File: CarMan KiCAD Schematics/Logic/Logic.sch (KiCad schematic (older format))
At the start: 50 parts, among them J1 Motor Controller Can Line, J2 NON-ISO I2C Testing Header, J3 Logic-TSI Connector, J4 GLV BOB, J5 PIC program, J6 NON-ISO CAN Testing, J7 You're Welcome -Ethan, U1 MCP9700AT-HTT-Sensor_Temperat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, U10 BNO_055, U11 Raspberry_Pi_RTC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

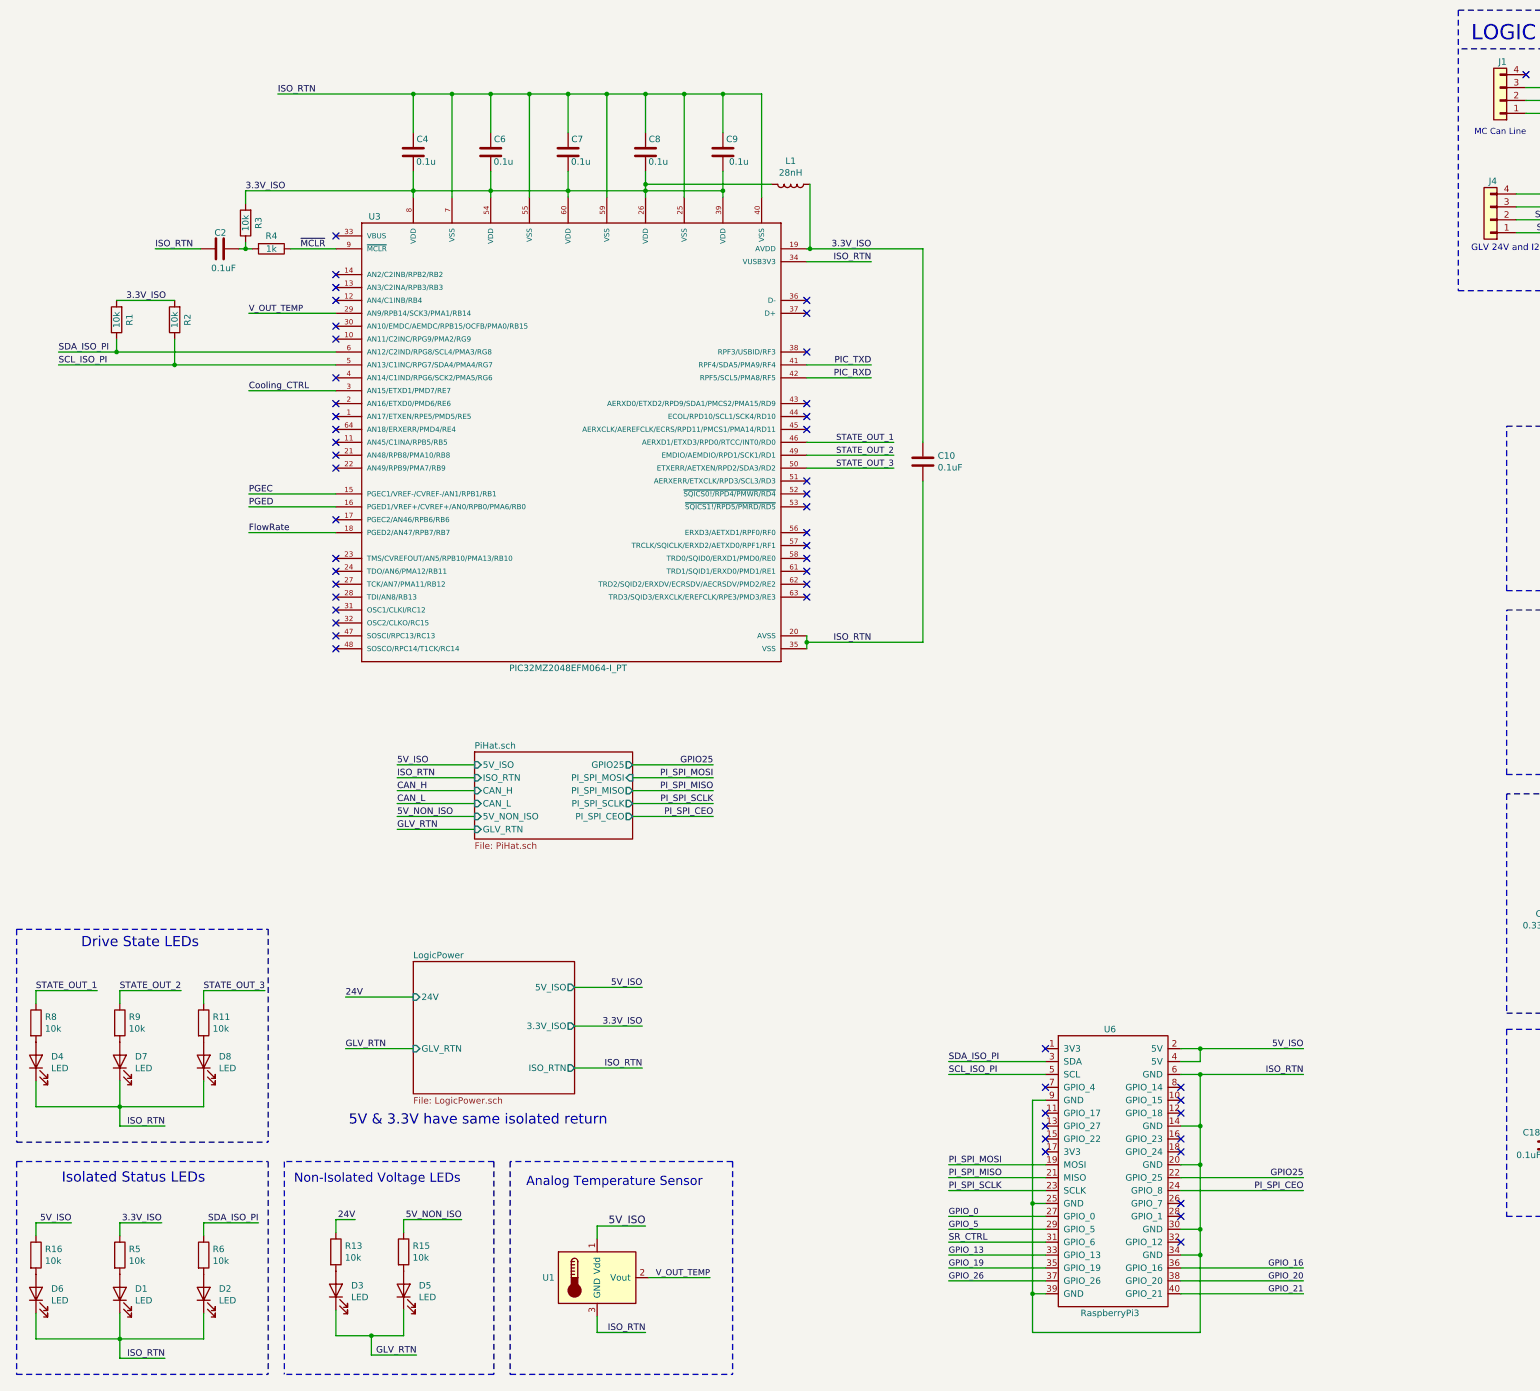
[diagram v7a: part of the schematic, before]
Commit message: -Added buttons across coils (instead of jumpers) for the AMS & IMD relays - Added push button for RTDS testing - Added a header (Currently J22) such that we can hook up a SPDT switch and change direction car is driving
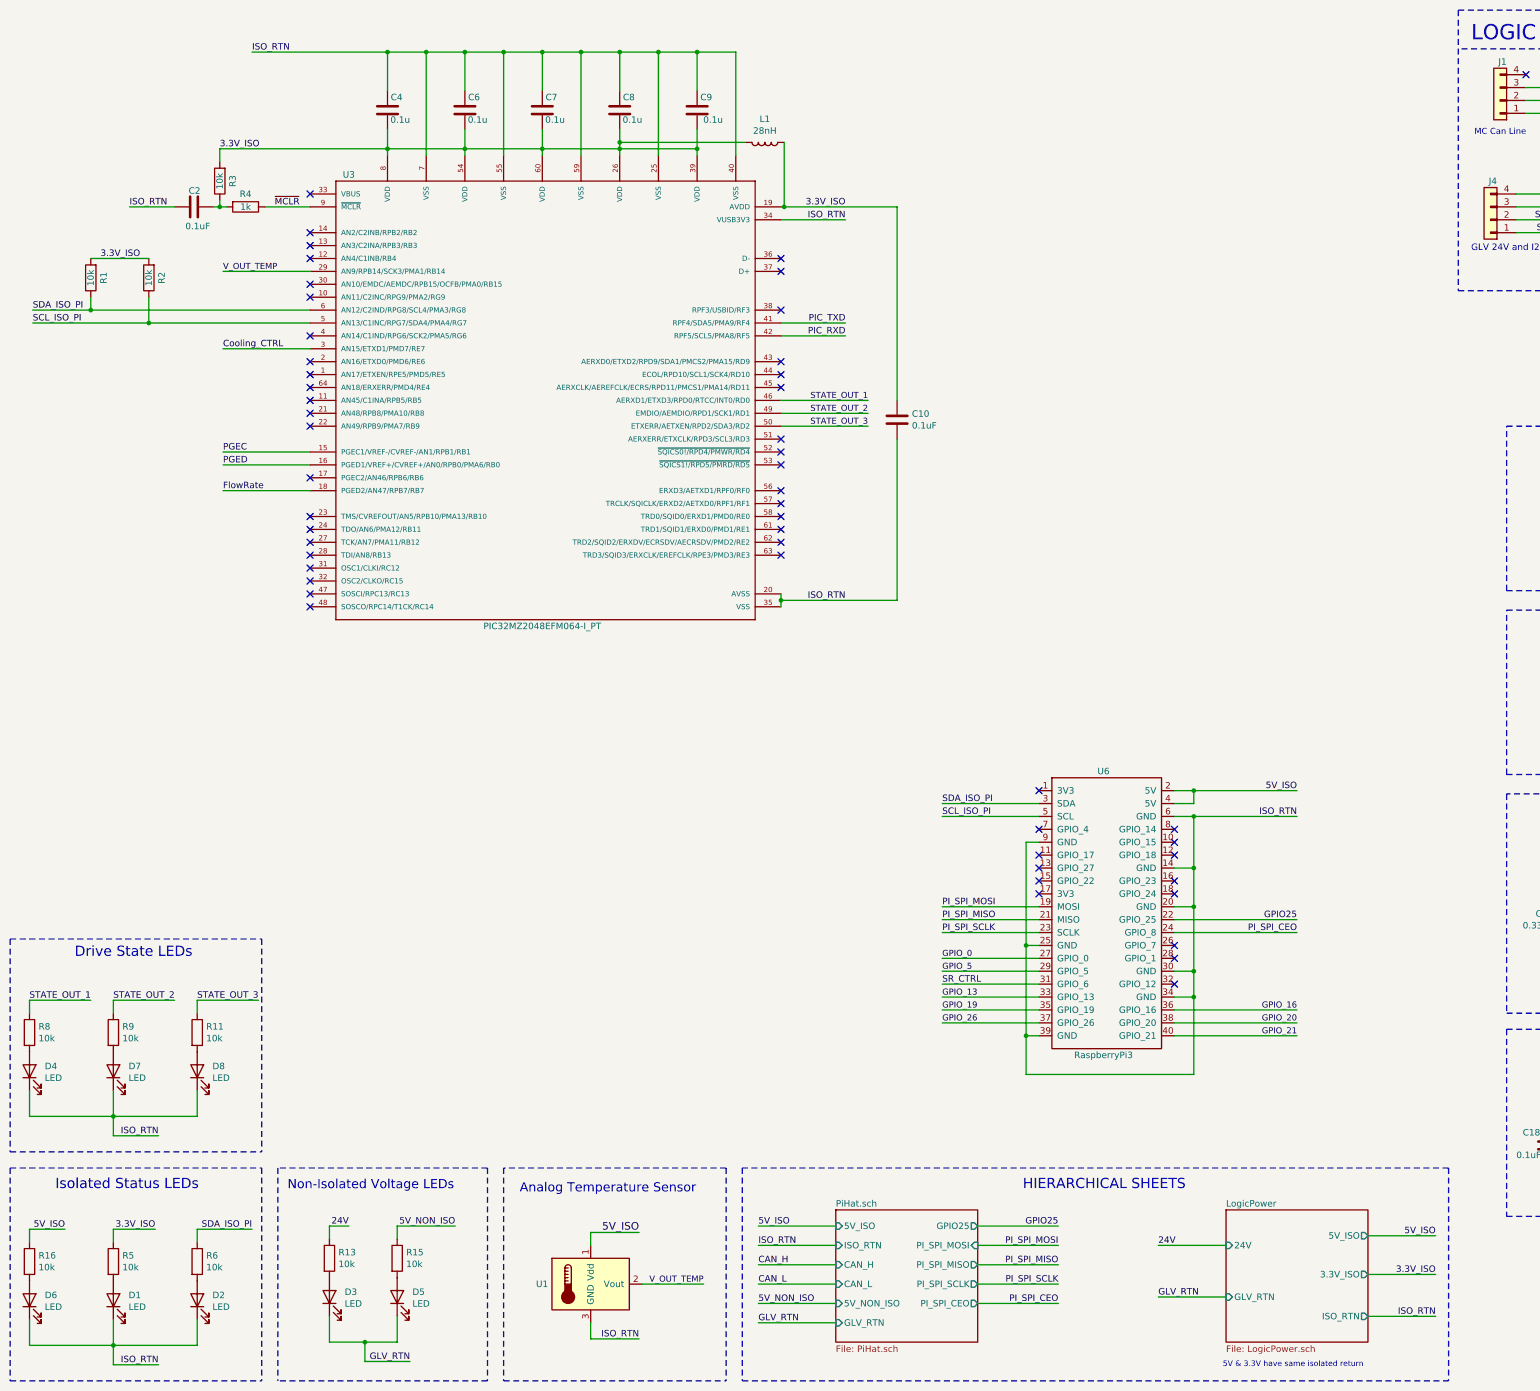
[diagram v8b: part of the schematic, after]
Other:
- note added: "HIERARCHICAL SHEETS"
- moved on the sheet: C10, C2, C4, C6, C7, C8, C9, D1, D2, D3, D4, D5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
